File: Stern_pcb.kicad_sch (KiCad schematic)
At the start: 2 parts, among them Q1 DMG3404L

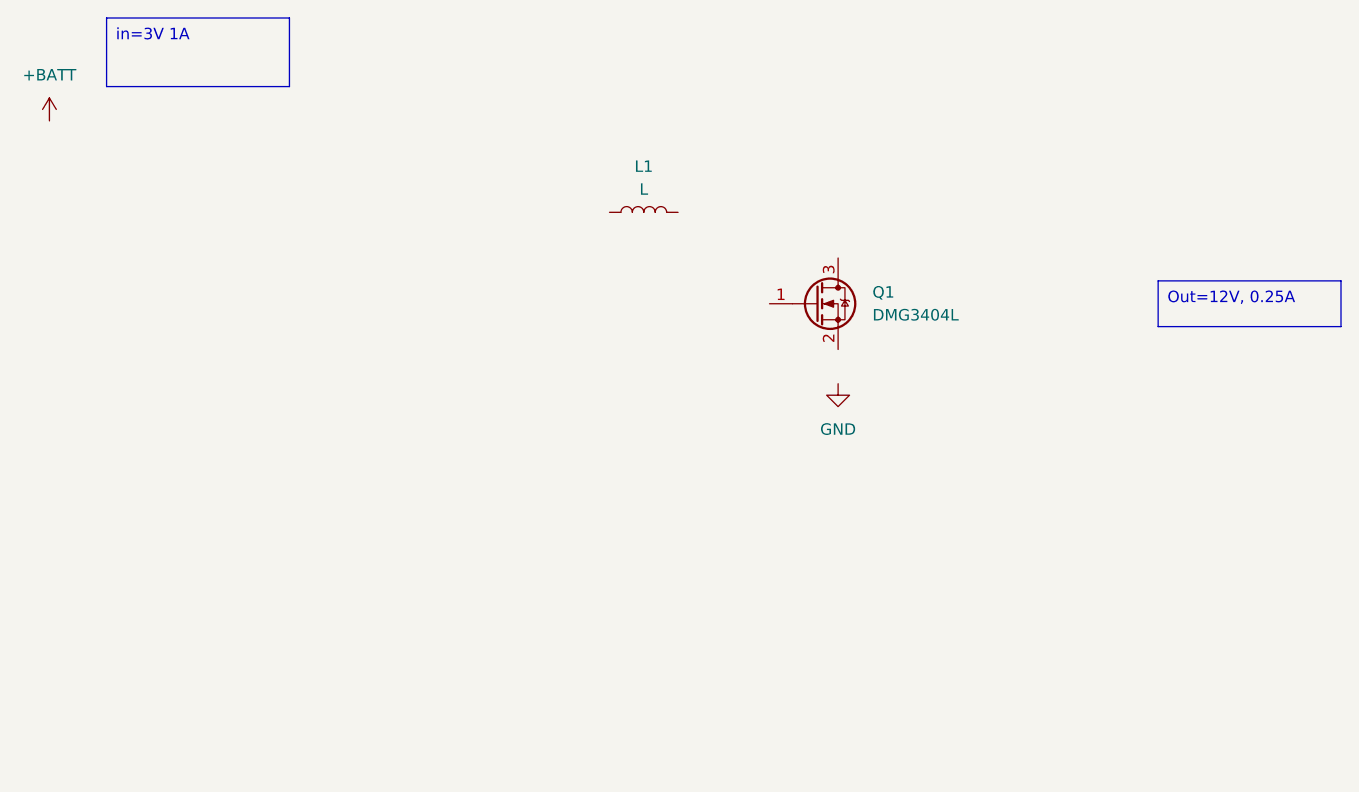
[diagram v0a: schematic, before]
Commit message: Updated USB-charger Schematics
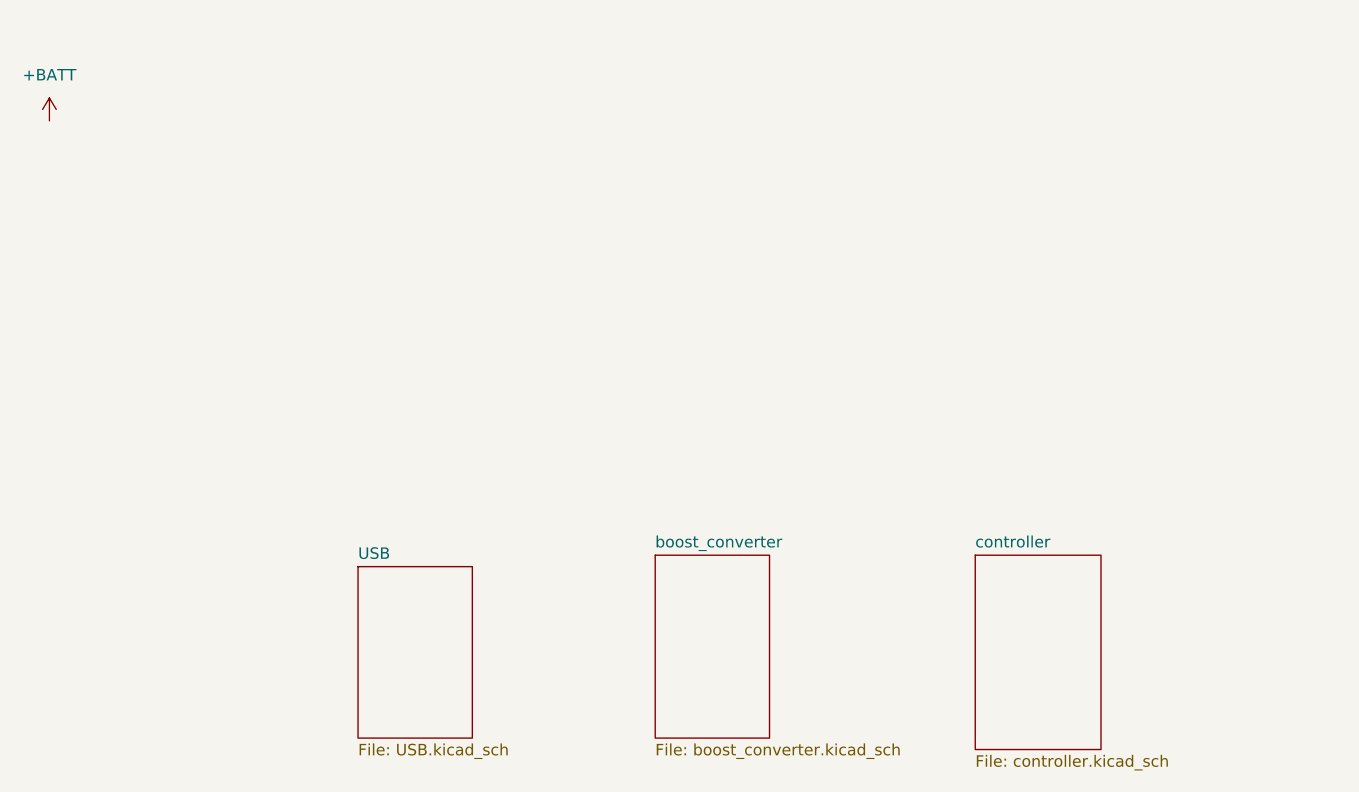
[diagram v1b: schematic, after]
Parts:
- removed L1: L, symbol Device:L
- removed Q1: DMG3404L, Package_TO_SOT_SMD:SOT-23, symbol Transistor_FET:DMG3404L
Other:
- added sheet USB (USB.kicad_sch)
- added sheet boost_converter (boost_converter.kicad_sch)
- added sheet controller (controller.kicad_sch)
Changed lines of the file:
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@@
 	(generator_version "8.0")
 	(paper "A4")
-	(text_box "Out=12V, 0.25A"
-		(exclude_from_sim no)
-		(at 212.09 73.66 0)
-		(size 20.32 5.08)
-		(stroke
-			(width 0)
-			(type default)
-		)
-		(fill
-			(type none)
-		)
-		(effects
-			(font
-				(size 1.27 1.27)
-			)
-			(justify left top)
-		)
-	)
-	(text_box "in=3V 1A"
-		(exclude_from_sim no)
-		(at 95.25 44.45 0)
-		(size 20.32 7.62)
-		(stroke
-			(width 0)
-			(type default)
-		)
-		(fill
-			(type none)
-		)
-		(effects
-			(font
-				(size 1.27 1.27)
-			)
-			(justify left top)
-		)
-	)
-	(symbol
-		(lib_id "power:GND")
-		(at 176.53 85.09 0)
-		(unit 1)
-		(exclude_from_sim no)
-		(in_bom yes)
-		(on_board yes)
-		(dnp no)
-		(fields_autoplaced yes)
-		(property "Reference" "#PWR01"
-			(at 176.53 91.44 0)
-			(effects
-				(font
-					(size 1.27 1.27)
-				)
-				(hide yes)
-			)
-		)
-		(property "Value" "GND"
-			(at 176.53 90.17 0)
-			(effects
-				(font
-					(size 1.27 1.27)
-				)
-			)
-		)
-		(property "Footprint" ""
-			(at 176.53 85.09 0)
-			(effects
-				(font
-					(size 1.27 1.27)
-				)
-				(hide yes)
-			)
-		)
-		(property "Datasheet" ""
-			(at 176.53 85.09 0)
-			(effects
-				(font
-					(size 1.27 1.27)
-				)
-				(hide yes)
-			)
-		)
-		(property "Description" "Power symbol creates a global label with name \"GND\" , ground"
-			(at 176.53 85.09 0)
-			(effects
-				(font
-					(size 1.27 1.27)
-				)
-				(hide yes)
-			)
-		)
-		(pin "1"
-		)
-		(instances
-			(project ""
-				(path "/96f7660e-d3d9-4022-bb72-d6467b6cbc1f"
-					(reference "#PWR01")
-					(unit 1)
-				)
-			)
-		)
-	)
 	(symbol
 		(lib_id "power:+BATT")
@@
 		)
 	)
-	(symbol
-		(lib_id "Transistor_FET:DMG3404L")
-		(at 173.99 76.2 0)
-		(unit 1)
-		(exclude_from_sim no)
-		(in_bom yes)
-		(on_board yes)
-		(dnp no)
+	(sheet
+		(at 156.21 104.14)
+		(size 12.7 20.32)
 		(fields_autoplaced yes)
-		(property "Reference" "Q1"
-			(at 180.34 74.9299 0)
+		(stroke
+			(width 0.1524)
+			(type solid)
+		)
+		(fill
+			(color 0 0 0 0.0000)
+		)
+		(property "Sheetname" "boost_converter"
+			(at 156.21 103.4284 0)
 			(effects
 				(font
 					(size 1.27 1.27)
 				)
-				(justify left)
+				(justify left bottom)
 			)
 		)
-		(property "Value" "DMG3404L"
-			(at 180.34 77.4699 0)
+		(property "Sheetfile" "boost_converter.kicad_sch"
+			(at 156.21 125.0446 0)
 			(effects
 				(font
 					(size 1.27 1.27)
 				)
-				(justify left)
+				(justify left top)
 			)
 		)
-		(property "Footprint" "Package_TO_SOT_SMD:SOT-23"
-			(at 179.07 78.105 0)
-			(effects
-				(font
-					(size 1.27 1.27)
-					(italic yes)
+		(instances
+			(project "Stern_pcb"
+				(path "/96f7660e-d3d9-4022-bb72-d6467b6cbc1f"
+					(page "3")
 				)
-				(justify left)
-				(hide yes)
 			)
 		)
-		(property "Datasheet" "http://www.diodes.com/assets/Datasheets/DMG3404L.pdf"
-			(at 179.07 80.01 0)
+	)
+	(sheet
+		(at 123.19 105.41)
+		(size 12.7 19.05)
+		(fields_autoplaced yes)
+		(stroke
+			(width 0.1524)
+			(type solid)
+		)
+		(fill
+			(color 0 0 0 0.0000)
+		)
+		(property "Sheetname" "USB"
+			(at 123.19 104.6984 0)
 			(effects
 				(font
 					(size 1.27 1.27)
 				)
-				(justify left)
-				(hide yes)
+				(justify left bottom)
 			)
 		)
-		(property "Description" "5.8A Id, 30V Vds, N-Channel MOSFET, SOT-23"
-			(at 173.99 76.2 0)
+		(property "Sheetfile" "USB.kicad_sch"
+			(at 123.19 125.0446 0)
 			(effects
 				(font
 					(size 1.27 1.27)
 				)
-				(hide yes)
+				(justify left top)
 			)
 		)
-		(pin "3"
-		)
-		(pin "1"
-		)
-		(pin "2"
-		)
 		(instances
-			(project ""
+			(project "Stern_pcb"
 				(path "/96f7660e-d3d9-4022-bb72-d6467b6cbc1f"
-					(reference "Q1")
-					(unit 1)
+					(page "3")
 				)
 			)
 		)
 	)
-	(symbol
-		(lib_id "Device:L")
-		(at 154.94 66.04 90)
-		(unit 1)
-		(exclude_from_sim no)
-		(in_bom yes)
-		(on_board yes)
-		(dnp no)
+	(sheet
+		(at 191.77 104.14)
+		(size 13.97 21.59)
 		(fields_autoplaced yes)
-		(property "Reference" "L1"
-			(at 154.94 60.96 90)
+		(stroke
+			(width 0.1524)
+			(type solid)
+		)
+		(fill
+			(color 0 0 0 0.0000)
+		)
+		(property "Sheetname" "controller"
+			(at 191.77 103.4284 0)
 			(effects
 				(font
 					(size 1.27 1.27)
 				)
+				(justify left bottom)
 			)
 		)
-		(property "Value" "L"
-			(at 154.94 63.5 90)
+		(property "Sheetfile" "controller.kicad_sch"
+			(at 191.77 126.3146 0)
 			(effects
 				(font
 					(size 1.27 1.27)
 				)
+				(justify left top)
 			)
 		)
-		(property "Footprint" ""
-			(at 154.94 66.04 0)
-			(effects
-				(font
-					(size 1.27 1.27)
-				)
-				(hide yes)
-			)
-		)
-		(property "Datasheet" "~"
-			(at 154.94 66.04 0)
-			(effects
-				(font
-					(size 1.27 1.27)
-				)
-				(hide yes)
-			)
-		)
-		(property "Description" "Inductor"
-			(at 154.94 66.04 0)
-			(effects
-				(font
-					(size 1.27 1.27)
-				)
-				(hide yes)
-			)
-		)
-		(pin "1"
-		)
-		(pin "2"
-		)
 		(instances
-			(project ""
+			(project "Stern_pcb"
 				(path "/96f7660e-d3d9-4022-bb72-d6467b6cbc1f"
-					(reference "L1")
-					(unit 1)
+					(page "4")
 				)
 			)

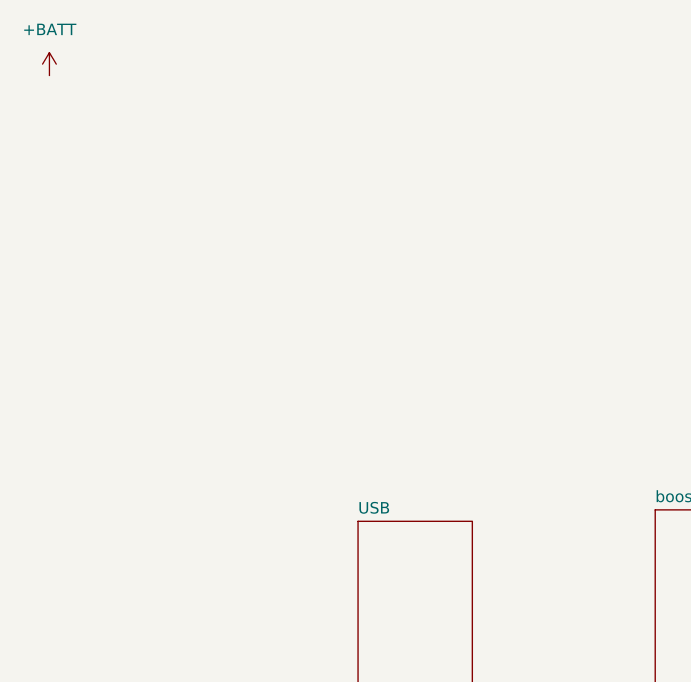
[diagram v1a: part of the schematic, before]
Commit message: assigned footprints
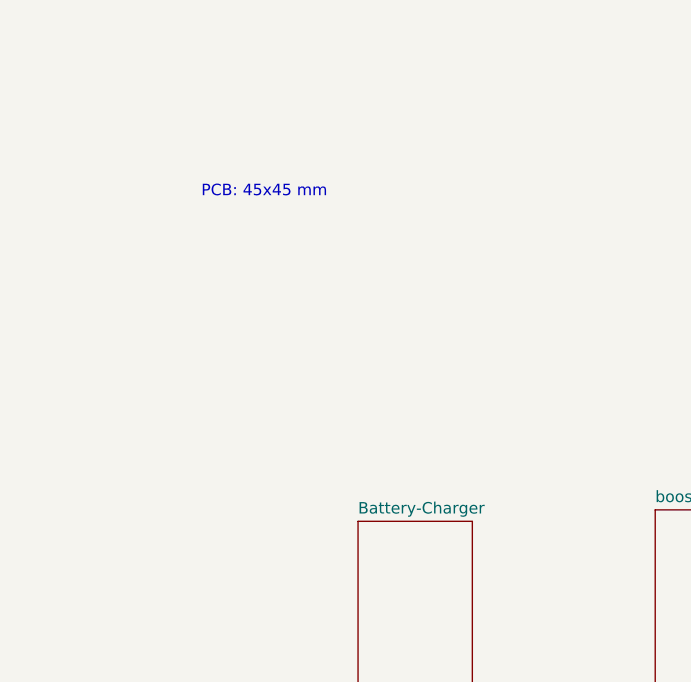
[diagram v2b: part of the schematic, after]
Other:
- sheet USB renamed Battery-Charger
- note added: "PCB: 45x45 mm"
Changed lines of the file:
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@@
 	(generator_version "8.0")
 	(paper "A4")
-	(symbol
-		(lib_id "power:+BATT")
-		(at 88.9 55.88 0)
-		(unit 1)
+	(text "PCB: 45x45 mm"
 		(exclude_from_sim no)
-		(in_bom yes)
-		(on_board yes)
-		(dnp no)
-		(fields_autoplaced yes)
-		(property "Reference" "#PWR02"
-			(at 88.9 59.69 0)
-			(effects
-				(font
-					(size 1.27 1.27)
-				)
-				(hide yes)
-			)
-		)
-		(property "Value" "+BATT"
-			(at 88.9 50.8 0)
-			(effects
-				(font
-					(size 1.27 1.27)
-				)
-			)
-		)
-		(property "Footprint" ""
-			(at 88.9 55.88 0)
-			(effects
-				(font
-					(size 1.27 1.27)
-				)
-				(hide yes)
-			)
-		)
-		(property "Datasheet" ""
-			(at 88.9 55.88 0)
-			(effects
-				(font
-					(size 1.27 1.27)
-				)
-				(hide yes)
-			)
-		)
-		(property "Description" "Power symbol creates a global label with name \"+BATT\""
-			(at 88.9 55.88 0)
-			(effects
-				(font
-					(size 1.27 1.27)
-				)
-				(hide yes)
-			)
-		)
-		(pin "1"
-		)
-		(instances
-			(project ""
-				(path "/96f7660e-d3d9-4022-bb72-d6467b6cbc1f"
-					(reference "#PWR02")
-					(unit 1)
-				)
+		(at 112.776 68.834 0)
+		(effects
+			(font
+				(size 1.27 1.27)
 			)
 		)
@@
 			(color 0 0 0 0.0000)
 		)
-		(property "Sheetname" "USB"
+		(property "Sheetname" "Battery-Charger"
 			(at 123.19 104.6984 0)
 			(effects
